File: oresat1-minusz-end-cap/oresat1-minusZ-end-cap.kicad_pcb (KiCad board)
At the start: 2 copper layers, 105.6 x 105.6 mm, 47 parts, among them J1 M55-7011242R, J2 U.FL-R-SMA, U1 LTC4305, U2 MMC5983MA, U3 MMC5983MA

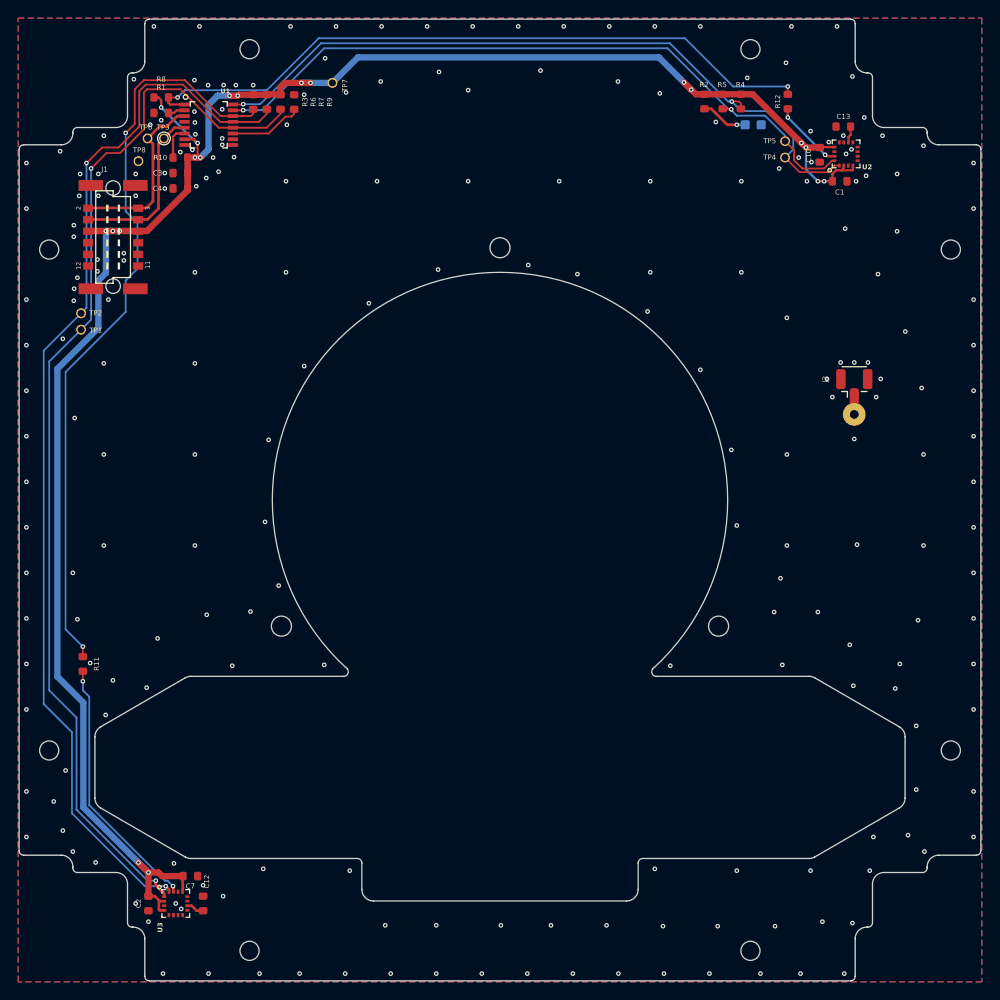
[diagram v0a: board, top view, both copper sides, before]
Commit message: RM 3100 board layout
Round 1 - awaiting design review. Some issues with GND pads; DRC is clean, but looks weird. Debating if U1 needs to be further in the corner, therefore change its layout completely.
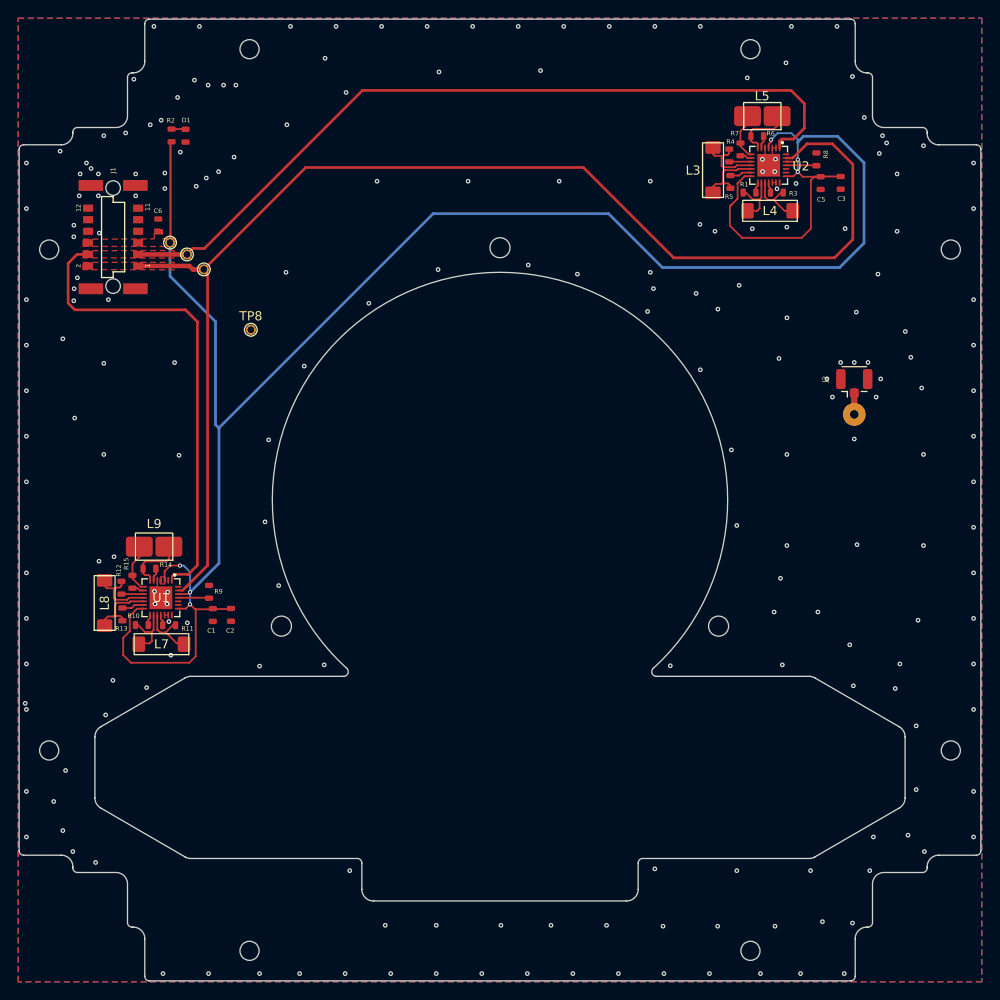
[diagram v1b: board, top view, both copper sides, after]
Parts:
- removed C10, C7: 100n, oresat0.5-minusz-end-cap:.0603-B-NOSILK
- removed C12, C13, C4: 10u, oresat0.5-minusz-end-cap:.0603-B-NOSILK
- removed D2: GRN, oresat0.5-minusz-end-cap:LED-0603
- removed TP1, TP2, TP4, TP5: Test-Point, oresat-misc:TestPoint-0.75mm-th
- removed U3: MMC5983MA, oresat-ics:LGA-16(3X3)
- added C5: 0.1u, oresat-passives:0603-C-NOSILK, F.Cu at (183.7, 70.2)
- added C6: 10u, oresat-passives:0603-C-NOSILK, F.Cu at (111.0, 74.8)
- added D1: GRN, oresat-passives:0603-C-NOSILK, F.Cu at (114.0, 65.0)
- added L3: SEN2-XY (y-axis), oresat-misc:RM3100 SEN-XY-f, F.Cu at (171.9, 68.8)
- added L4: SEN2-XY (x-axis), oresat-misc:RM3100 SEN-XY-f, F.Cu at (178.2, 73.2)
- added L5: SEN2-Z (z-axis), oresat-misc:RM3100 SEN-Z-f, F.Cu at (177.3, 62.9)
- added L7: SEN1-XY (x-axis), oresat-misc:RM3100 SEN-XY-f, F.Cu at (111.3, 120.8)
- added L8: SEN1-XY (y-axis), oresat-misc:RM3100 SEN-XY-f, F.Cu at (105.1, 116.3)
- added L9: SEN1-Z (z-axis), oresat-misc:RM3100 SEN-Z-f, F.Cu at (110.5, 110.1)
- added R13: 121, oresat-passives:0603-C-NOSILK, F.Cu at (107.0, 117.6)
- added R14: 121, oresat-passives:0603-C-NOSILK, F.Cu at (110.0, 112.5)
- added R15: 121, oresat-passives:0603-C-NOSILK, F.Cu at (108.1, 114.0)
- C1: value 100n -> 0.1u; footprint oresat0.5-minusz-end-cap:.0603-B-NOSILK -> oresat-passives:0603-C-NOSILK
- C2, C3: value 100n -> 10u; footprint oresat0.5-minusz-end-cap:.0603-B-NOSILK -> oresat-passives:0603-C-NOSILK
- J1: footprint oresat0.5-minusz-end-cap:HARWIN-M55-70X1242R -> oresat-connectors:J-Harwin-M55-60X1242R
- R1, R10, R3, R4, R5, R6, R7: value 4.7k -> 121; footprint oresat0.5-minusz-end-cap:.0603-B-NOSILK -> oresat-passives:0603-C-NOSILK
- R11, R12: value 2.7k -> 121; footprint oresat0.5-minusz-end-cap:.0603-B-NOSILK -> oresat-passives:0603-C-NOSILK
- R2: footprint oresat0.5-minusz-end-cap:.0603-B-NOSILK -> oresat-passives:0603-C-NOSILK
- R8, R9: value 4.7k -> ~; footprint oresat0.5-minusz-end-cap:.0603-B-NOSILK -> oresat-passives:0603-C-NOSILK
- TP6, TP7, TP8: moved to F.Cu
- U1: value LTC4305 -> ~; footprint oresat-ics:16-SSOP -> oresat-misc:RM3100-MagI2C
- U2: value MMC5983MA -> ~; footprint oresat-ics:LGA-16(3X3) -> oresat-misc:RM3100-MagI2C
- moved R12 90.6 mm to (106.9, 114.6), turned to -90 degrees
- moved C1 83.7 mm to (117.0, 117.6), turned to -90 degrees
- moved C3 72.5 mm to (185.9, 70.2), turned to -90 degrees
- moved R8 72.3 mm to (183.2, 67.6), turned to -90 degrees
- moved R1 65.2 mm to (175.9, 71.2)
- moved R2 58.6 mm to (112.4, 65.0), turned to -90 degrees
- moved R3 58.4 mm to (178.9, 71.2), turned to 180 degrees
- moved R9 54.6 mm to (116.6, 115.1)
- moved R6 54.0 mm to (176.8, 65.0), turned to 0 degrees
- moved U1 52.2 mm to (111.3, 115.7), turned to 180 degrees
- moved R10 51.5 mm to (109.2, 118.7)
- moved R7 50.8 mm to (174.9, 66.5), turned to -90 degrees
- moved C2 33.0 mm to (119.0, 117.6)
- moved TP7 25.0 mm to (112.3, 76.7), turned to 0 degrees
- moved TP8 22.2 mm to (121.1, 86.3)
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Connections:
- C1 pad 1: +3.3V -> +3.3v
- C2 pad 1: +3.3V -> +3.3v
- C3 pad 1: +3.3V -> +3.3v
- J1 pad 5: +3.3V -> +3.3v
- J1 pad 6: +3.3V -> +3.3v
- R1 pad 1: GND -> Net-(U2-XINP)
- R1 pad 2: Net-(U1-~{ALERT}) -> Net-(U2-XDRVP)
- R10 pad 1: Net-(U1-ENABLE) -> Net-(U1-XINP)
- R10 pad 2: +3.3V -> Net-(U1-XDRVP)
- R11 pad 1: Net-(U3-INT) -> Net-(U1-XINN)
- R11 pad 2: Net-(U1-~{ALERT1}) -> Net-(U1-XDRVN)
- R12 pad 1: Net-(U2-INT) -> Net-(U1-YINP)
- R12 pad 2: Net-(U1-~{ALERT2}) -> Net-(U1-YDRVP)
- R2 pad 2: +3.3V -> +3.3v
- R3 pad 1: Net-(U1-~{ALERT1}) -> Net-(U2-XINN)
- R3 pad 2: +3.3V -> Net-(U2-XDRVN)
- R4 pad 1: /SCL2 -> Net-(U2-YINP)
- R4 pad 2: +3.3V -> Net-(U2-YDRVP)
- R5 pad 1: /SDA2 -> Net-(U2-YINN)
- R5 pad 2: +3.3V -> Net-(U2-YDRVN)
- R6 pad 1: /SDA1 -> Net-(U2-ZINP)
- R6 pad 2: +3.3V -> Net-(U2-ZDRVP)
- R7 pad 1: /SCL1 -> Net-(U2-ZINN)
- R7 pad 2: +3.3V -> Net-(U2-ZDRVN)
- R8 pad 1: Net-(U1-~{ALERT2}) -> GND
- R8 pad 2: +3.3V -> Net-(U2-REXT)
- R9 pad 2: Net-(U1-READY) -> Net-(U1-REXT)
- TP7 pad 1: +3.3V -> +3.3v
- U1 pad 1: Net-(U1-~{ALERT2}) -> /MAG-SCL
- U1 pad 10: unconnected-(U1-ADR2-Pad10) -> Net-(U1-YDRVP)
- U1 pad 11: Net-(U1-READY) -> Net-(U1-YINP)
- U1 pad 12: /SCL1 -> Net-(U1-YINN)
- U1 pad 13: /SDA1 -> Net-(U1-YDRVN)
- U1 pad 14: Net-(U1-~{ALERT1}) -> +3.3v
- U1 pad 15: /SDA2 -> Net-(U1-XDRVP)
- U1 pad 16: /SCL2 -> Net-(U1-XINP)
- U1 pad 2: Net-(U1-~{ALERT}) -> GND
- U1 pad 3: /MAG-SDA -> +3.3v
- U1 pad 4: GND -> +3.3v
- U1 pad 5: /MAG-SCL -> GND
- U1 pad 6: Net-(U1-ENABLE) -> Net-(U1-ZDRVP)
- U1 pad 7: +3.3V -> Net-(U1-ZINP)
- U1 pad 8: unconnected-(U1-ADR0-Pad8) -> Net-(U1-ZINN)
- U1 pad 9: unconnected-(U1-ADR1-Pad9) -> Net-(U1-ZDRVN)
- U2 pad 1: /SCL2 -> /MAG-SCL
- U2 pad 10: Net-(U2-CAP) -> Net-(U2-YDRVP)
- U2 pad 11: GND -> Net-(U2-YINP)
- U2 pad 12: unconnected-(U2-NC-Pad12) -> Net-(U2-YINN)
- U2 pad 13: +3.3V -> Net-(U2-YDRVN)
- U2 pad 14: unconnected-(U2-NC-Pad14) -> +3.3v
- U2 pad 15: Net-(U2-INT) -> Net-(U2-XDRVP)
- U2 pad 16: /SDA2 -> Net-(U2-XINP)
- U2 pad 2: +3.3V -> GND
- U2 pad 3: unconnected-(U2-NC-Pad3) -> GND
- U2 pad 4: +3.3V -> +3.3v
- U2 pad 5: unconnected-(U2-SPI_SDO-Pad5) -> GND
- U2 pad 6: unconnected-(U2-NC-Pad6) -> Net-(U2-ZDRVP)
- U2 pad 7: unconnected-(U2-NC-Pad7) -> Net-(U2-ZINP)
- U2 pad 8: unconnected-(U2-NC-Pad8) -> Net-(U2-ZINN)
- U2 pad 9: GND -> Net-(U2-ZDRVN)
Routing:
- net +3.3v: track 0.00 -> 230.0 mm, vias 0 -> 6
- net +3.3V: track 217.1 -> 0.00 mm, vias 19 -> 0
- net /MAG-SDA: track 19.7 -> 142.4 mm
- net /MAG-SCL: track 18.9 -> 140.5 mm
- net /SCL1: track 117.3 -> 0.00 mm, vias 2 -> 0
- net /SDA1: track 117.2 -> 0.00 mm, vias 2 -> 0
- net Net-(U1-~{ALERT1}): track 83.0 -> 0.00 mm, vias 2 -> 0
- net /SCL2: track 79.8 -> 0.00 mm, vias 2 -> 0
- net /SDA2: track 76.7 -> 0.00 mm, vias 2 -> 0
- net Net-(U1-~{ALERT2}): track 76.2 -> 0.00 mm, vias 2 -> 0
- net Net-(U3-INT): track 28.5 -> 0.00 mm, vias 2 -> 0
- net Net-(U1-READY): track 8.12 -> 0.00 mm
- net Net-(U2-INT): track 7.84 -> 0.00 mm, vias 2 -> 0
- net Net-(U1-YINP): track 0.00 -> 7.73 mm
- net Net-(U2-YINP): track 0.00 -> 7.73 mm
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- added copper zone on F.Cu, net +3.3v
- added copper zone on F.Cu, net /MAG-SCL
- added copper zone on F.Cu, net /MAG-SDA
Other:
- copper layers 2 -> 4

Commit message: Polishing the schematic and layout
Cleaned up ERCs, lots of OCD polishing for no reason, added 3.3V zone, cleaned up 3.3V routing.
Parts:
- added C4: 100n, oresat-passives:0603-C-NOSILK, F.Cu at (179.9, 64.7)
- added C7: 100n, oresat-passives:0603-C-NOSILK, F.Cu at (119.2, 113.7)
- C1, C5: value 0.1u -> 100n
- C2: value 10u -> ~; footprint oresat-passives:0603-C-NOSILK -> oresat-passives:0805-C-NOSILK
- C3, C6: footprint oresat-passives:0603-C-NOSILK -> oresat-passives:0805-C-NOSILK
- D1, R2: moved to B.Cu
- R8, R9: value ~ -> 33k
- U1, U2: value ~ -> RM3100
- moved C3 12.3 mm to (174.1, 73.4)
- moved TP8 10.5 mm to (112.2, 80.9)
- moved C5 3.03 mm to (182.8, 67.3), turned to 0 degrees
- moved R8 1.82 mm to (182.0, 69.0), turned to 90 degrees
- moved D1 1.54 mm to (112.4, 65.0)
- moved R2 1.52 mm to (114.0, 65.0)
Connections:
- U1 pad 28: GND -> +3.3v
- U1 pad 3: +3.3v -> GND
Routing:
- net +3.3v: track 230.0 -> 10.8 mm, vias 6 -> 16
- net /MAG-SCL: track 140.5 -> 127.1 mm, vias 0 -> 2
- net /MAG-SDA: track 142.4 -> 133.7 mm
- net GND: track 7.42 -> 14.4 mm
- net Net-(U2-REXT): track 3.35 -> 2.12 mm
- net (no net): vias 4 -> 0
- added copper zone on In2.Cu, net +3.3v
- added copper zone on In1.Cu, net GND
- added copper zone on In2.Cu, net GND
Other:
- board text added: "${ISSUE_DATE}"
- board text added: "${TITLE} v${REVISION}"
- board text added: "GPS"
- board text removed: "2024/03/20"
- board text removed: "OreSat0.5 -Z End Cap v1.2"

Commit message: Fix BOM and add 3D of antenna.
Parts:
- C2: value ~ -> 10u

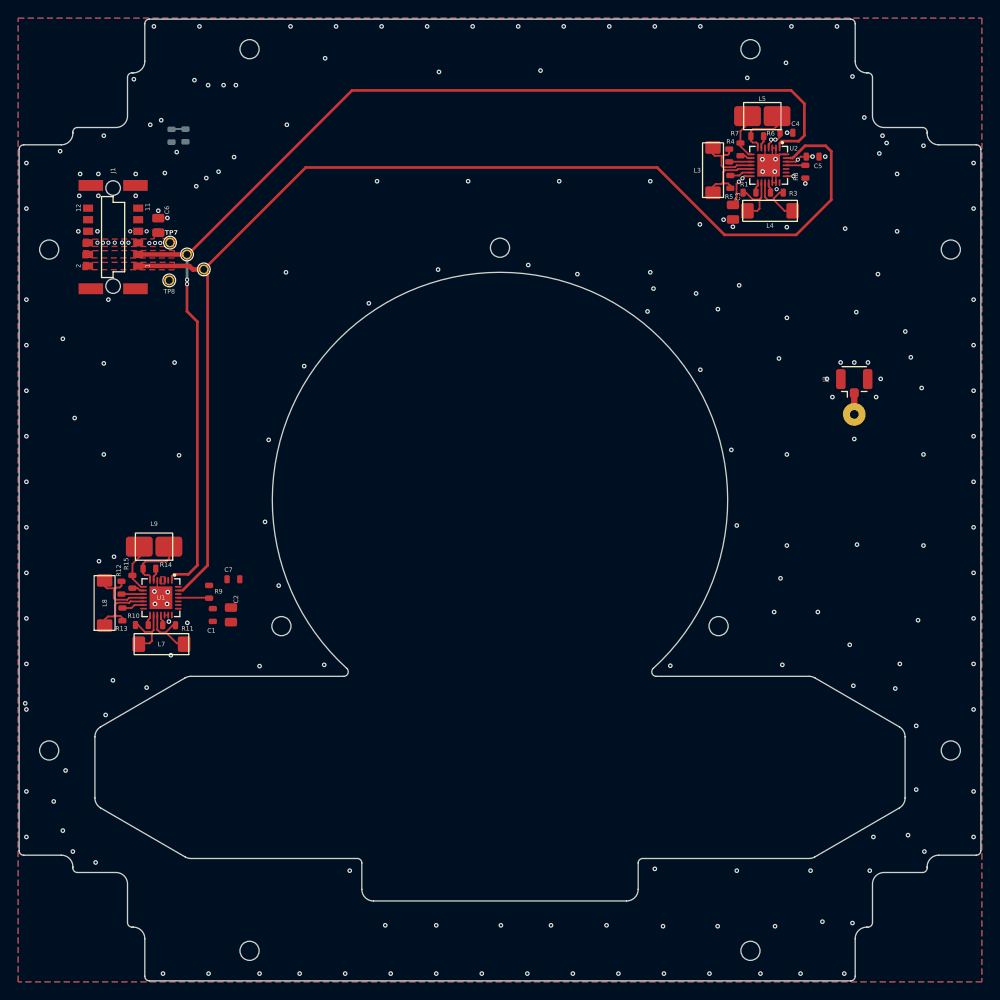
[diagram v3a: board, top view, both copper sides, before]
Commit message: New -Z DFX
Added new DFX to edge.cuts and User.comments. Antenna footprint warning - juts out over cut.
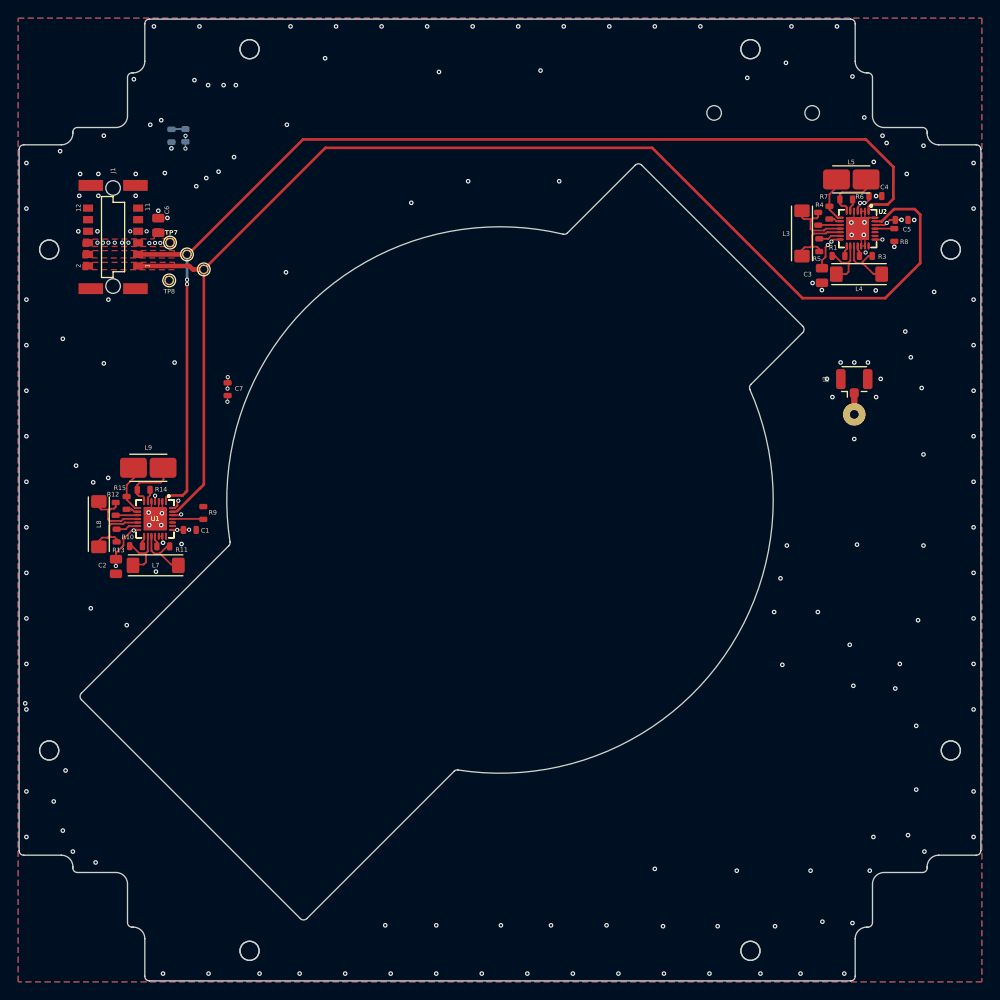
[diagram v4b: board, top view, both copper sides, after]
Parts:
- removed the REF** at (148.5, 77.3)
- removed the REF** at (99.0, 77.5)
- removed the REF** at (124.5, 118.8)
- removed the REF** at (176.0, 55.5)
- removed the REF** at (172.5, 118.8)
- added REF**: MountingHole_2.1mm, MountingHole:MountingHole_2.1mm, B.Cu at (99.0, 77.5)
- added REF**: MountingHole_2.1mm, MountingHole:MountingHole_2.1mm, B.Cu at (176.0, 55.5)
- added U1: RM3100, oresat-misc:RM3100-MagI2C, F.Cu at (110.6, 107.1)
- added U2: RM3100, oresat-misc:RM3100-MagI2C, F.Cu at (187.8, 75.2)
- moved LOGO1 71.7 mm to (177.3, 129.3)
- moved C7 20.9 mm to (118.6, 92.8), turned to -90 degrees
- moved C2 13.7 mm to (106.3, 112.3)
- moved C4 12.0 mm to (189.7, 71.6)
- moved L3 12.0 mm to (181.7, 75.7)
- moved R4 12.0 mm to (183.4, 74.1)
- moved R5 12.0 mm to (183.6, 77.0)
- moved R6 12.0 mm to (186.5, 72.0)
- moved U2 12.0 mm to (187.8, 75.2)
- moved C5 12.0 mm to (192.6, 74.2)
- moved L4 12.0 mm to (187.9, 80.2)
- moved R1 12.0 mm to (185.7, 78.2)
- moved R3 12.0 mm to (188.7, 78.2)
- moved R7 12.0 mm to (184.7, 73.5)
- moved R8 12.0 mm to (191.8, 75.9)
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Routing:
- net +3.3v: track 10.8 -> 23.6 mm, vias 16 -> 27
- net /MAG-SDA: track 133.7 -> 139.4 mm
- net GND: track 14.4 -> 18.9 mm, vias 211 -> 180
- net /MAG-SCL: track 127.1 -> 126.0 mm
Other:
- outline, holes or cut-outs redrawn

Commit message: Added 3D models and fixed fab des
3D models of antenna patch (-Z) and M55 connector & magIc2 chip on both boards.
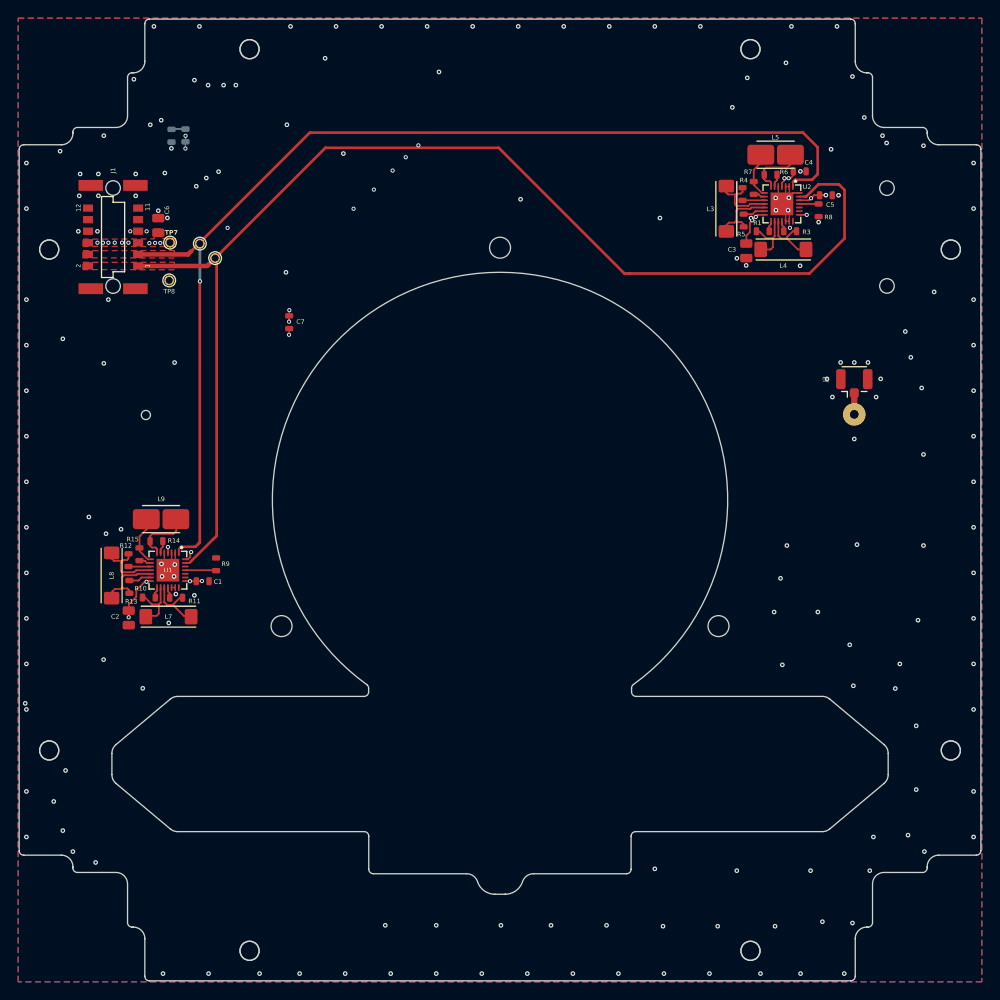
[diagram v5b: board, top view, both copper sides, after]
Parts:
- removed the U1 at (110.6, 107.1)
- removed the U2 at (187.8, 75.2)
- moved LOGO1 16.4 mm to (187.2, 116.2)
- moved C7 9.99 mm to (125.3, 85.5)
- moved L3 8.74 mm to (173.3, 73.0)
- moved R4 8.74 mm to (175.1, 71.4)
- moved C3 8.74 mm to (175.5, 77.6)
- moved C4 8.74 mm to (181.4, 68.9)
- moved C5 8.74 mm to (184.3, 71.5)
- moved L5 8.74 mm to (178.8, 67.1)
- moved R5 8.74 mm to (175.2, 74.3)
- moved R6 8.74 mm to (178.2, 69.3)
- moved U2 8.74 mm to (179.5, 72.5)
- moved L4 8.74 mm to (179.6, 77.5)
- moved R1 8.74 mm to (177.4, 75.5)
- moved R3 8.74 mm to (180.4, 75.5)
- moved R7 8.74 mm to (176.4, 70.7)
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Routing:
- net /MAG-SDA: track 139.4 -> 136.9 mm
- net /MAG-SCL: track 126.0 -> 123.7 mm, vias 2 -> 1
- net +3.3v: track 23.6 -> 22.6 mm, vias 27 -> 26
- net GND: vias 180 -> 185
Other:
- outline, holes or cut-outs redrawn
